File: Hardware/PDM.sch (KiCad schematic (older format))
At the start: 28 parts, among them J1 Conn_01x40_Male, J2 Conn_01x06_Male, J3 Conn_01x08_Male, Q1 Q_NMOS_GSD, SW1 SW_Push, U1 STM32F446RETx, Y1 16MHz, Y2 Crystal

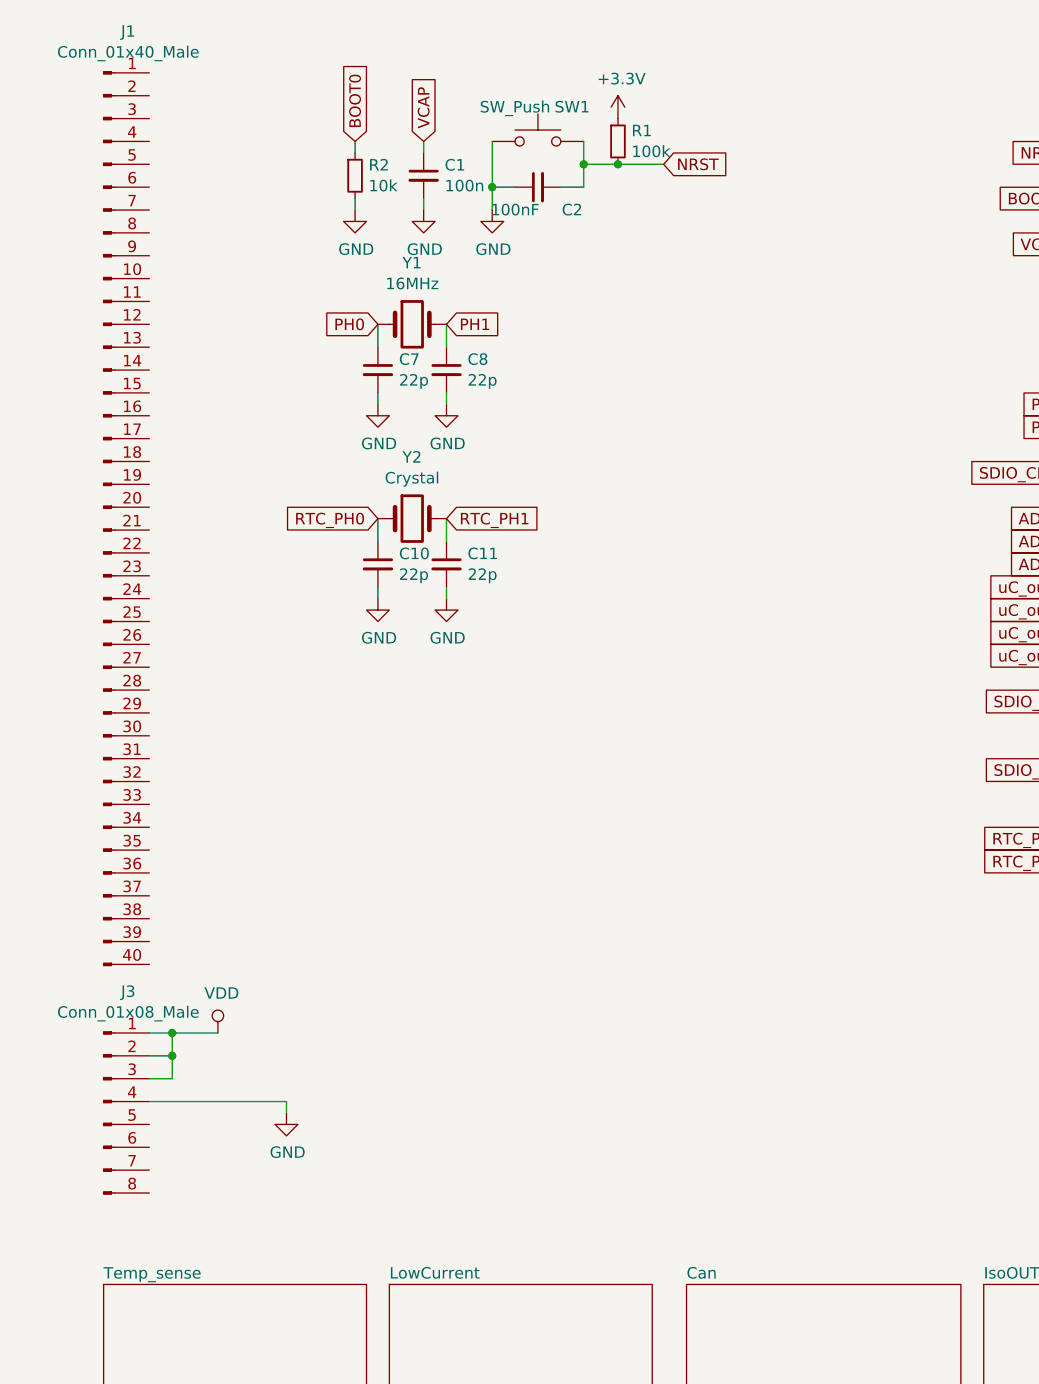
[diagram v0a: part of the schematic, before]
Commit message: passive components changed to 0603 and Main connector configuration set
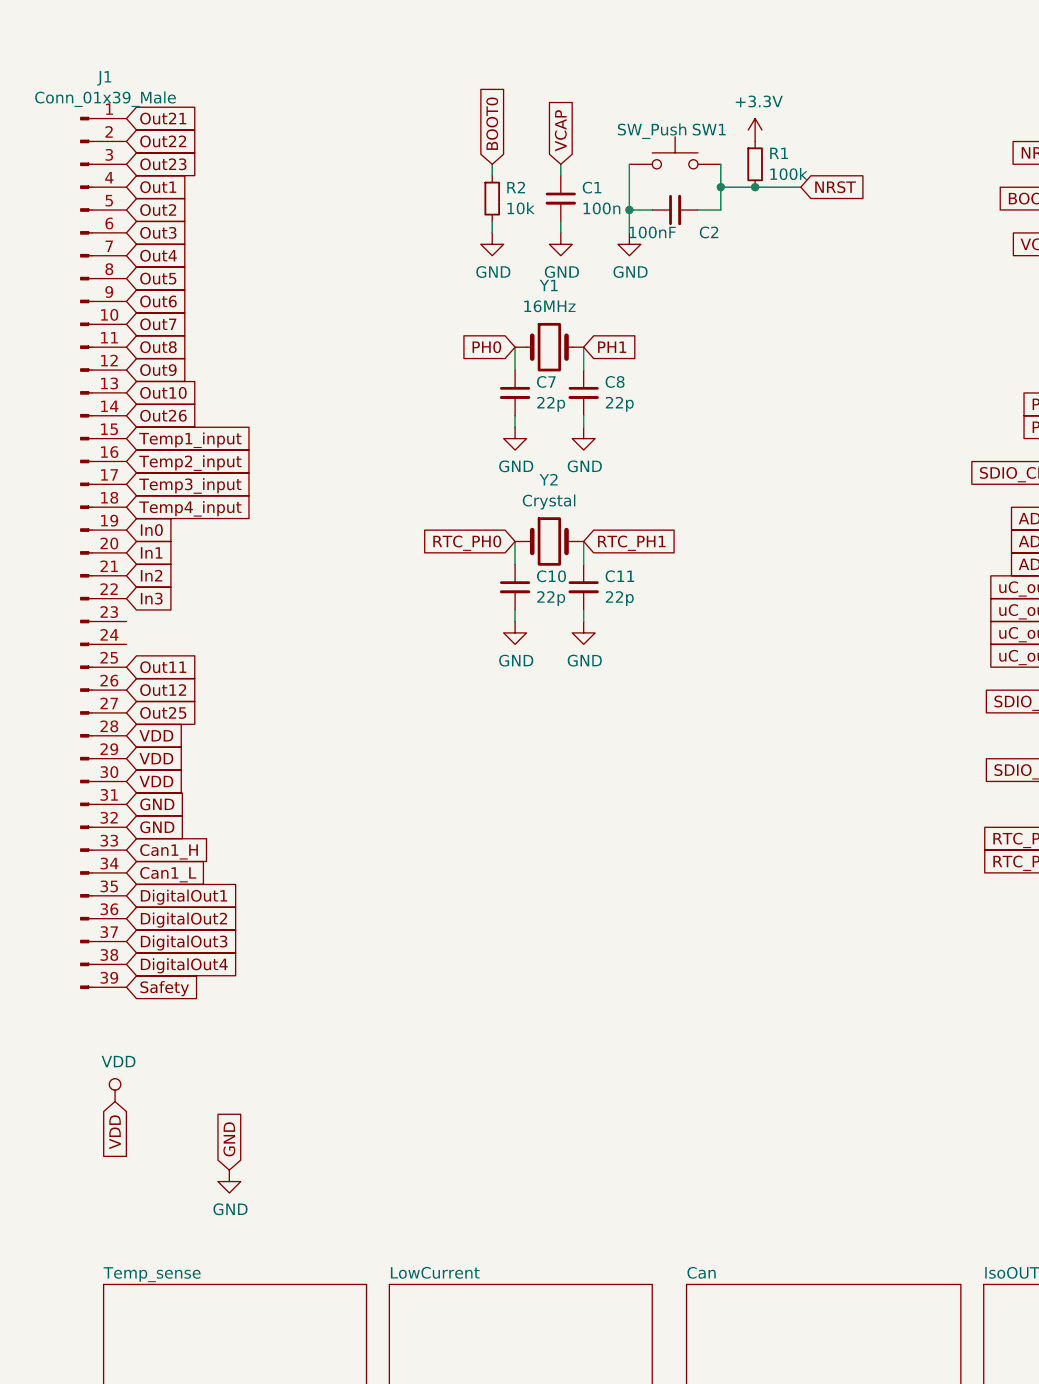
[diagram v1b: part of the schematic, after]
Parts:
- removed J1: Conn_01x40_Male, symbol Connector:Conn_01x40_Male
- removed J3: Conn_01x08_Male, symbol Connector:Conn_01x08_Male
- added J1: Conn_01x39_Male, FCI39pin:39pinFCI_ECU, symbol Connector:Conn_01x39_Male
- C1, C10, C11, C12, C2, C3, C4, C5, C6, C7, C8, C9: footprint Capacitor_SMD:C_0805_2012Metric -> Capacitor_SMD:C_0603_1608Metric
- R1, R2, R3, R4, R5: footprint Resistor_SMD:R_0805_2012Metric -> Resistor_SMD:R_0603_1608Metric
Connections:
- net GND: now also J1.31 (Pin_31), J1.32 (Pin_32)
- net VDD: now also J1.28 (Pin_28), J1.29 (Pin_29), J1.30 (Pin_30)
- new net Can1_H: J1.33 (Pin_33)
- new net Can1_L: J1.34 (Pin_34)
- new net DigitalOut1: J1.35 (Pin_35)
- new net DigitalOut2: J1.36 (Pin_36)
- new net DigitalOut3: J1.37 (Pin_37)
- new net DigitalOut4: J1.38 (Pin_38)
- new net In0: J1.19 (Pin_19)
- new net In1: J1.20 (Pin_20)
- new net In2: J1.21 (Pin_21)
- new net In3: J1.22 (Pin_22)
- new net Out1: J1.4 (Pin_4)
- new net Out10: J1.13 (Pin_13)
- new net Out11: J1.25 (Pin_25)
- new net Out12: J1.26 (Pin_26)
- new net Out2: J1.5 (Pin_5)
- new net Out21: J1.1 (Pin_1)
- new net Out22: J1.2 (Pin_2)
- new net Out23: J1.3 (Pin_3)
- new net Out25: J1.27 (Pin_27)
- new net Out26: J1.14 (Pin_14)
- new net Out3: J1.6 (Pin_6)
- new net Out4: J1.7 (Pin_7)
- new net Out5: J1.8 (Pin_8)
- new net Out6: J1.9 (Pin_9)
- new net Out7: J1.10 (Pin_10)
- new net Out8: J1.11 (Pin_11)
- new net Out9: J1.12 (Pin_12)
- new net Safety: J1.39 (Pin_39)
- new net Temp1_input: J1.15 (Pin_15)
- new net Temp2_input: J1.16 (Pin_16)
- new net Temp3_input: J1.17 (Pin_17)
- new net Temp4_input: J1.18 (Pin_18)
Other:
- moved on the sheet: C1, C10, C11, C2, C7, C8, R1, R2, SW1, Y1, Y2
